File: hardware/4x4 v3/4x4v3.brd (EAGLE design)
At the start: 89.2 x 36.7 mm, 44 parts, among them IC1 PIC18F2480-I/SP, J1 USB1035-XX-X-X-X-B_REVE, T1 BC547, T2 BC547, T3 BC547, T4 BC547, U1 IR3315, U2 IR3315, U3 IR3315, U4 IR3315

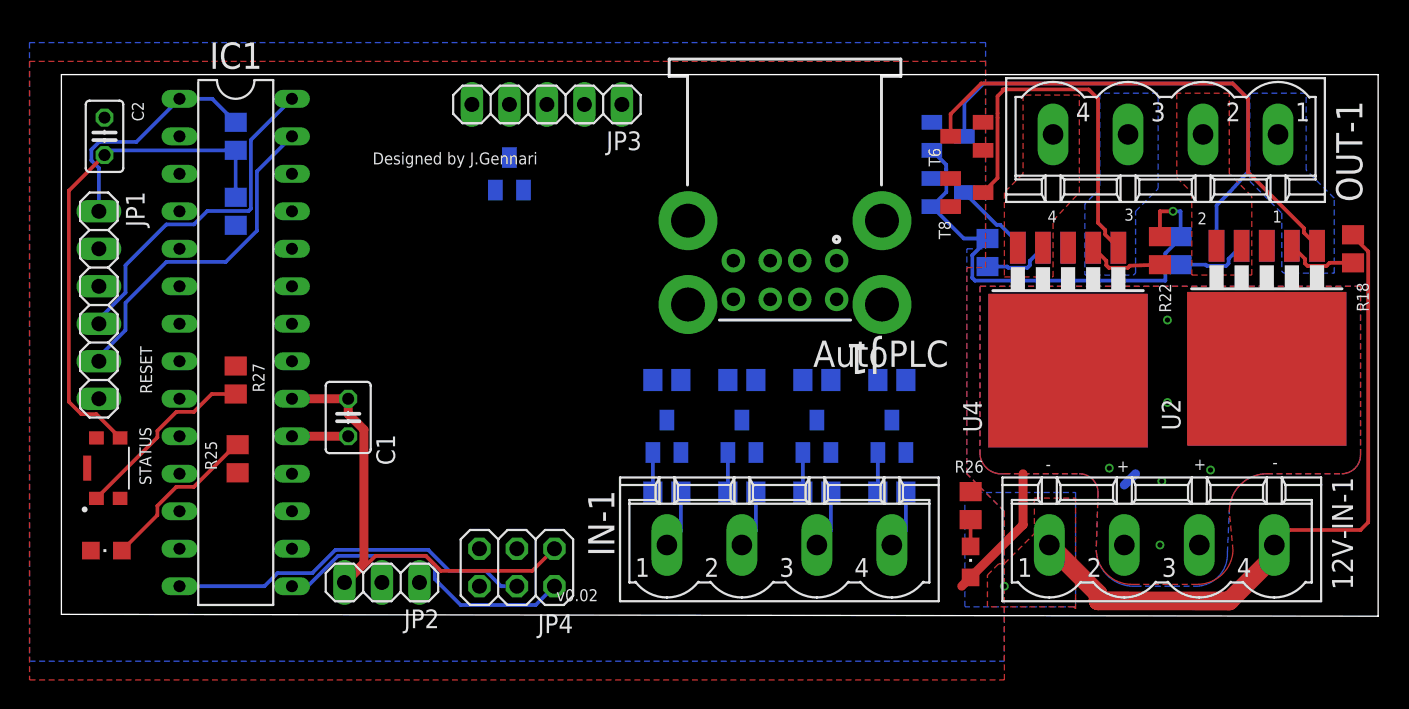
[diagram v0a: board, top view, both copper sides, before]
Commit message: Added ext board
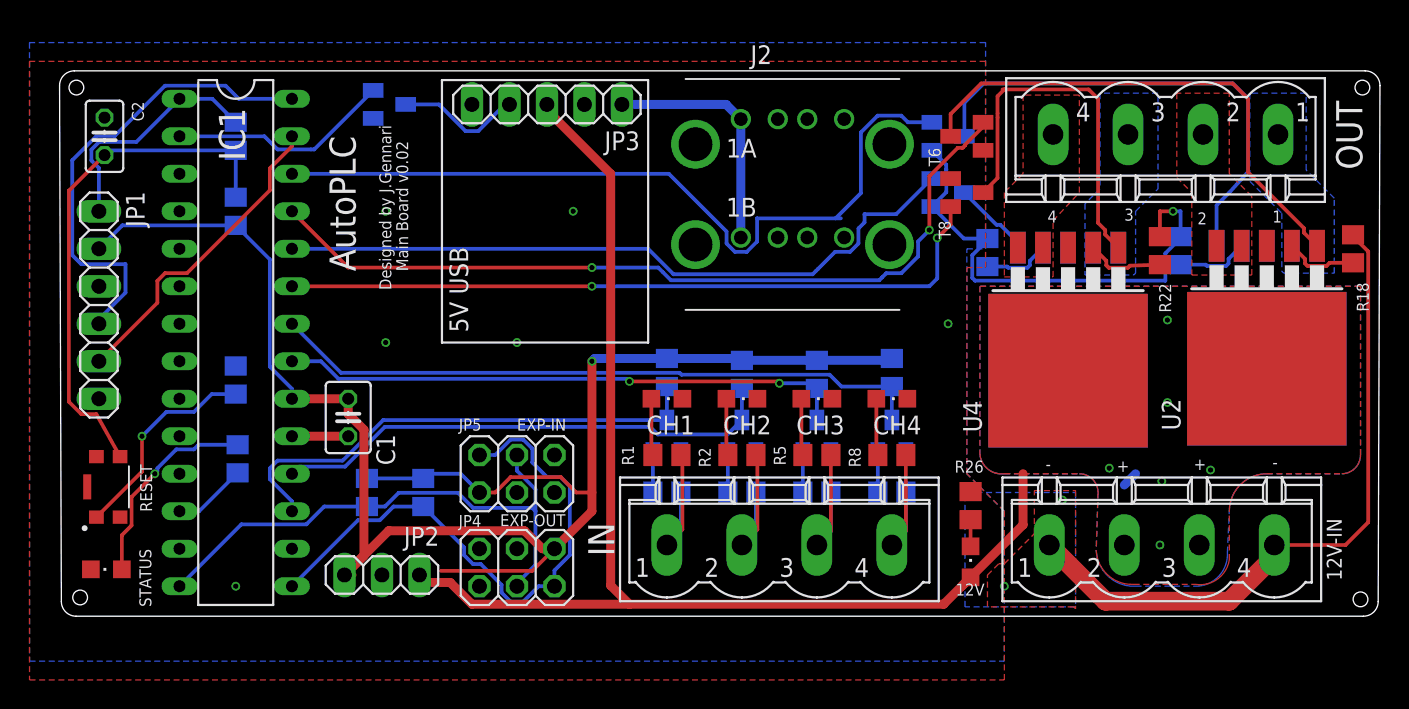
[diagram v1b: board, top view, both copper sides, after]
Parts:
- removed J1: USB1035-XX-X-X-X-B_REVE, USB1035-XX-X-X-X-B_REVE:GCT_USB1035-XX-X-X-X-B_REVE
- added J2: (no value), InputOutputIO (rev17e):614008235023
- added JP5: (no value), pinhead:2X03
- added LED1, LED2, LED3, LED5: (no value), led:CHIPLED_0805
- added R1, R14, R17, R2, R5, R8: (no value), resistor:R0805
- moved T9 9.39 mm to (46.0, 47.9), turned to 90 degrees
- moved LED9 1.27 mm to (26.8, 16.4)
- moved S1 1.27 mm to (26.9, 22.0)
- moved JP2 0.51 mm to (45.5, 16.0)
- moved R15 0.51 mm to (80.0, 29.7), turned to 270 degrees
- moved R6 0.51 mm to (64.8, 29.7), turned to 270 degrees
- moved R12 0.38 mm to (74.9, 29.6), turned to 270 degrees
- moved R9 0.38 mm to (69.8, 29.6), turned to 270 degrees
- flipped R25 to the bottom
- flipped R27 to the bottom
- renumbered 12V-IN-1 to 12V-IN, IN-1 to IN, OUT-1 to OUT
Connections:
- net 12V-1 renamed 12V
- net OUT-1-1 renamed OUT-1
- net OUT-1-2 renamed OUT-2
- net OUT-1-3 renamed OUT-3
- net OUT-1-4 renamed OUT-4
- net SIGIN-1-1 renamed SIGIN-1
- net SIGIN-1-2 renamed SIGIN-2
- net SIGIN-1-3 renamed SIGIN-3
- net SIGIN-1-4 renamed SIGIN-4
- removed net IN-1-1: IN.1, R4.1
- removed net IN-1-2: IN.2, R7.1
- removed net IN-1-3: IN.3, R10.1
- removed net IN-1-4: IN.4, R13.1
- removed net OUT-1-5: J1.1A, J1.1B, JP3.1
- removed net SIGOUT-1-1: IC1.5, T5.B
- removed net SIGOUT-1-2: IC1.4, T6.B
- removed net SIGOUT-1-3: IC1.3, T7.B
- removed net SIGOUT-1-4: IC1.2, T8.B
- removed net SIGOUT-1-5: T9.B
- new net IN-1: IN.1, R1.1, R4.1
- new net IN-2: IN.2, R2.1, R7.1
- new net IN-3: IN.3, R10.1, R5.1
- new net IN-4: IN.4, R13.1, R8.1
- new net N$3: LED5.A, R1.2
- new net N$5: LED1.A, R2.2
- new net N$7: LED2.A, R5.2
- new net N$9: LED3.A, R8.2
- new net OUT-5: J2.A1, J2.B1, JP3.1
- new net SIGOUT-1: IC1.26, T5.B
- new net SIGOUT-2: IC1.25, T6.B
- new net SIGOUT-3: IC1.24, T7.B
- new net SIGOUT-4: IC1.23, T8.B
- new net SIGOUT-5: IC1.2, T9.B
- net GND: now also J2.A4, J2.B4, J2.SHELL, J2.SHELL1, J2.SHELL2, J2.SHELL3, JP5.3, LED1.C, LED2.C, LED3.C, LED5.C; no longer J1.10, J1.11, J1.12, J1.4A, J1.4B, J1.9
- net SCL: now also JP5.4, R17.1
- net SDA: now also JP5.2, R14.2
- net VCC: now also JP5.1, R14.1, R17.2
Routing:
- net VCC: track 33.3 -> 115.8 mm, vias 0 -> 1
- net 12V: track 10.4 -> 85.5 mm
- net SIGOUT-2: track 0.00 -> 56.1 mm, vias 0 -> 2
- net SIGOUT-1: track 0.00 -> 53.7 mm
- net SIGOUT-4: track 0.00 -> 49.2 mm, vias 0 -> 2
- net SIGOUT-3: track 0.00 -> 47.7 mm
- net SIGIN-4: track 0.00 -> 44.7 mm
- net SIGIN-3: track 0.00 -> 38.5 mm, vias 0 -> 2
- net SIGIN-2: track 0.00 -> 34.6 mm
- net SIGIN-1: track 0.00 -> 34.1 mm
- net SDA: track 21.1 -> 39.3 mm
- net OUT-5: track 0.00 -> 16.5 mm
- net SIGOUT-5: track 0.00 -> 15.1 mm
- net SCL: track 24.9 -> 37.2 mm
- net IN-2: track 0.00 -> 10.5 mm
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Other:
- board size 89.2 x 36.7 mm -> 89.5 x 36.9 mm
- board text added: "12V"
- board text added: "CH1"
- board text added: "CH2"
- board text added: "CH3"
- board text added: "CH4"
- board text added: "EXP-IN"
- board text added: "EXP-OUT"
- board text added: "Main Board v0.02"
- board text removed: "v0.02"
